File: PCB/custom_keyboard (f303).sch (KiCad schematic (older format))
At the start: 374 parts, among them J1 Conn_01x04, J2 SM04B-SRSS-TB(LF)(SN), J3 Conn_01x03, Q1 2N7002, SW1 SW_Push, U1 SRV05-4, U12 XC6206P332MR, U14 STM32F303CBT6, X1 TestPoint_Small, X2 TestPoint_Small, Y2 8MHz

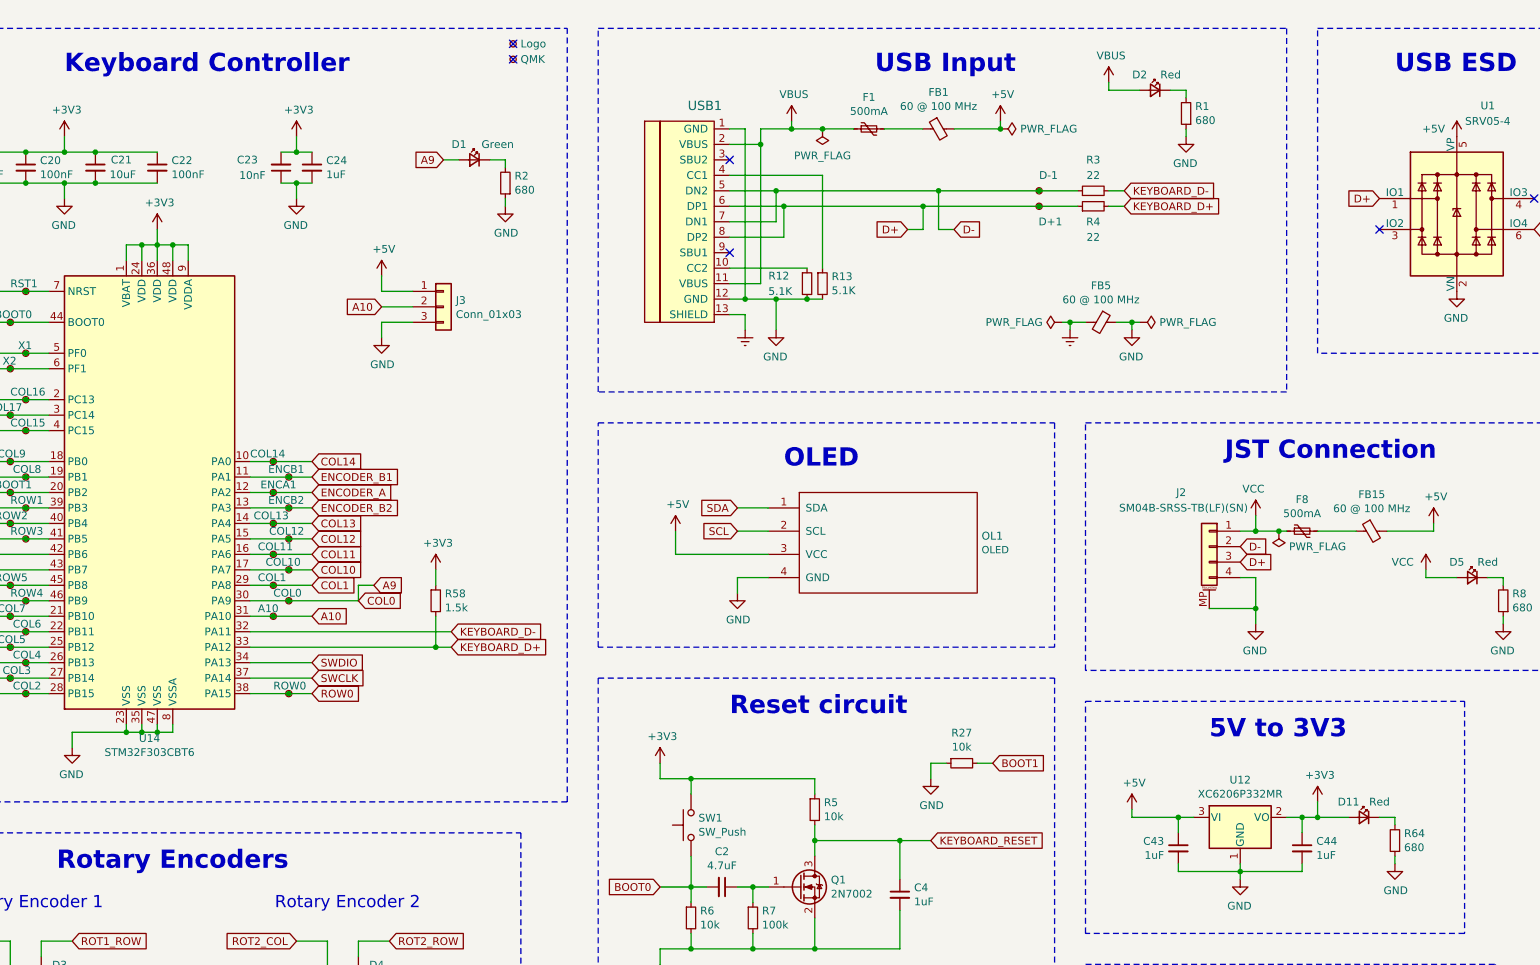
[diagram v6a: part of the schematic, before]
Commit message: Tweaked indicator LED circuit
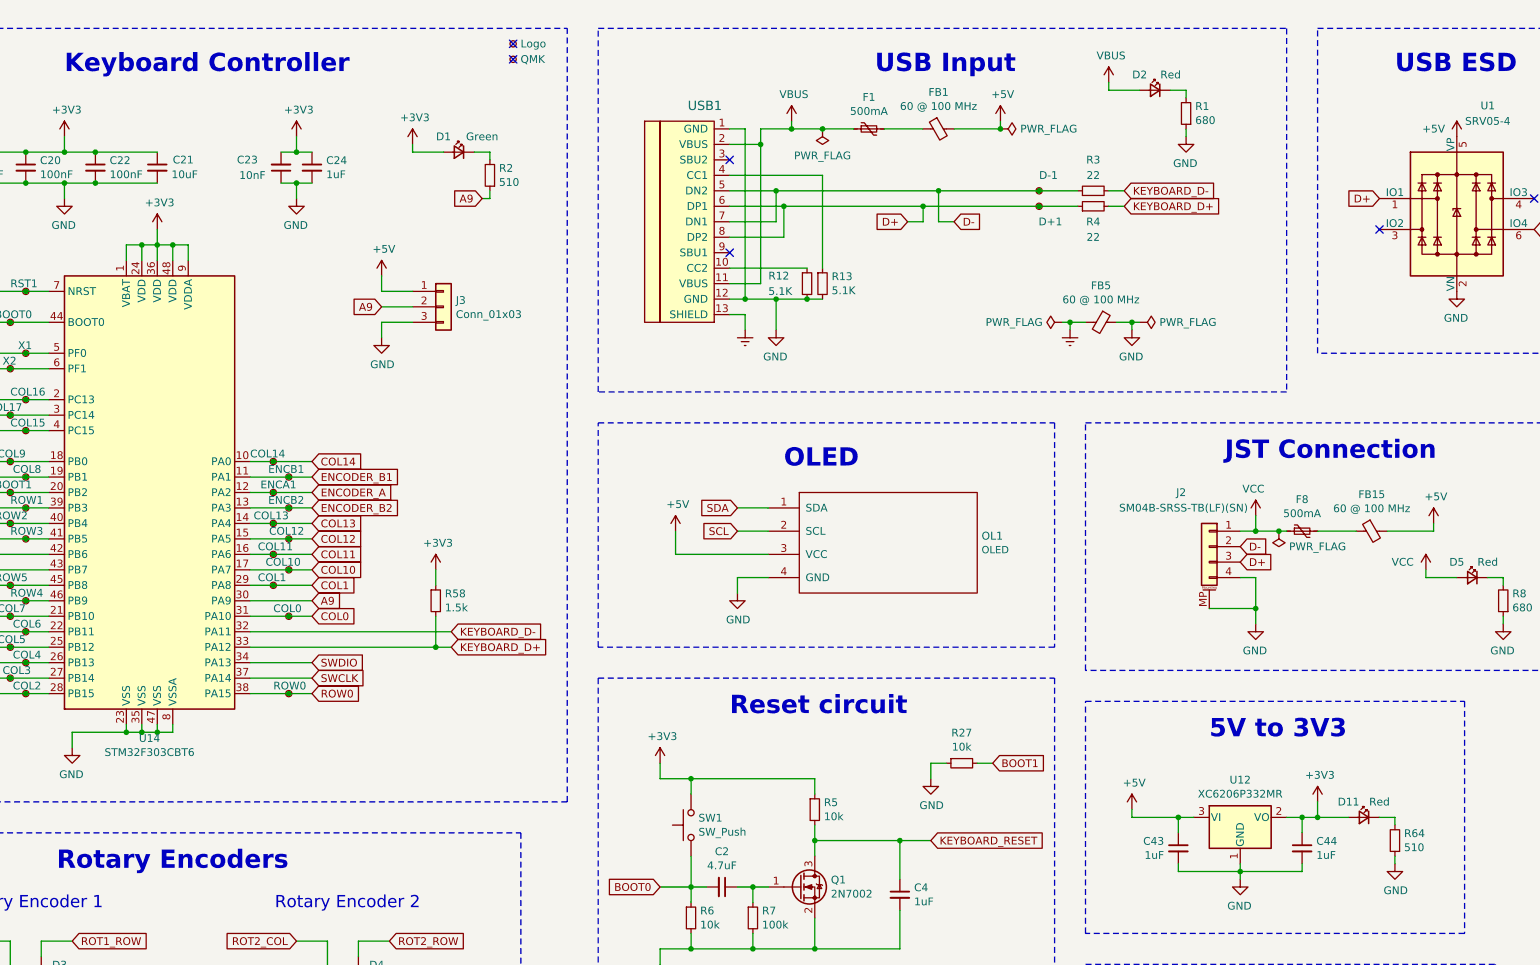
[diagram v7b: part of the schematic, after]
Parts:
- removed A10: TestPoint_Small, TestPoint:TestPoint_THTPad_D1.0mm_Drill0.5mm, symbol Connector:TestPoint_Small
- C1, C11, C13, C18, C19, C20, C22, C6, C8, C9: LCSC Part C49678 -> C28233
- LED1: footprint custom-footprints:MHT151RGBCT_with_outline -> custom-footprints:MHT151RGBCT
- R2, R64: value 680 -> 510; LCSC Part C17798 -> C17734
- Y2: footprint Crystal:Crystal_SMD_HC49-SD -> Crystal:Crystal_SMD_5032-2Pin_5.0x3.2mm; LCSC Part C12674 -> C115962
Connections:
- net +3V3: now also D1.2 (A)
- net A9: now also J3.2 (Pin_2), R2.1; no longer COL0.1, D1.2 (A), MX15.1, MX33.1, MX51.1, MX65.1, MX79.1, ROT1.S1
- net GND: no longer R2.1
- net A10 renamed COL0
- net COL0: now also COL0.1, MX15.1, MX33.1, MX51.1, MX65.1, MX79.1, ROT1.S1; no longer J3.2 (Pin_2)
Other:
- moved on the sheet: C21, C22, COL0, D1, R2

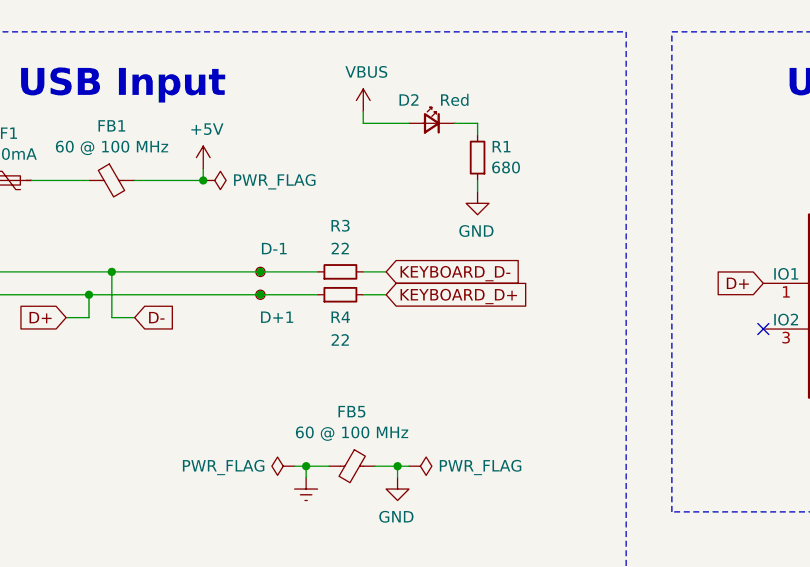
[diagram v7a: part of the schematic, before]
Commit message: Removed 22ohm resistors
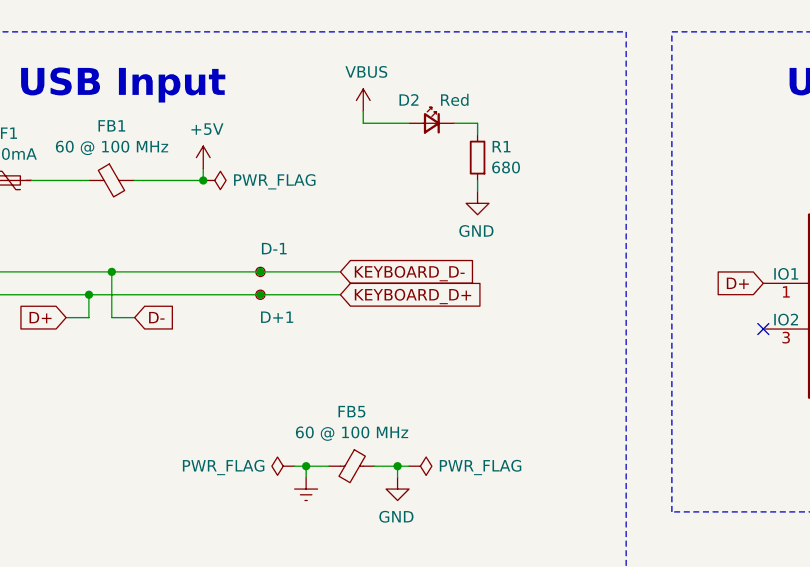
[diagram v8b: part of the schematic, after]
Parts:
- removed R3, R4: 22, Resistor_SMD:R_0805_2012Metric, symbol Device:R_Small
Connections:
- net KEYBOARD_D+ is gone; now on net D+: R58.2, U14.33 (PA12)
- net KEYBOARD_D- is gone; now on net D-: U14.32 (PA11)
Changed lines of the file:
@@
 Wire Notes Line
 	14150 9150 14150 11500
-Text GLabel 13100 10200 2    50   Input ~ 0
+Text GLabel 12900 10200 2    50   Input ~ 0
 KEYBOARD_D-
-Text GLabel 13100 10300 2    50   Input ~ 0
+Text GLabel 12900 10300 2    50   Input ~ 0
 KEYBOARD_D+
 $Comp
-L Device:R_Small R4
-U 1 1 A4110F3E
-P 12900 10300
-F 0 "R4" V 12800 10300 50  0000 C CNN
-F 1 "22" V 12700 10300 50  0000 C CNN
-F 2 "Resistor_SMD:R_0805_2012Metric" H 12900 10300 50  0001 C CNN
-F 3 "~" H 12900 10300 50  0001 C CNN
-F 4 "C17561" H 12900 10300 50  0001 C CNN "LCSC Part"
-	1    12900 10300
-	0    -1   -1   0
-$EndComp
-$Comp
-L Device:R_Small R3
-U 1 1 A4111764
-P 12900 10200
-F 0 "R3" V 13100 10200 50  0000 C CNN
-F 1 "22" V 13000 10200 50  0000 C CNN
-F 2 "Resistor_SMD:R_0805_2012Metric" H 12900 10200 50  0001 C CNN
-F 3 "~" H 12900 10200 50  0001 C CNN
-F 4 "C17561" H 12900 10200 50  0001 C CNN "LCSC Part"
-	1    12900 10200
-	0    -1   -1   0
-$EndComp
-$Comp
 L Connector:TestPoint_Small D-1
 U 1 1 6277D888
@@
 $EndComp
 Connection ~ 12550 10200
-Wire Wire Line
-	12550 10200 12800 10200
 Connection ~ 12550 10300
-Wire Wire Line
-	12550 10300 12800 10300
 $Comp
 L Connector:TestPoint_Small D+1
@@
 $EndComp
 Wire Wire Line
-	13000 10200 13100 10200
-Wire Wire Line
-	13000 10300 13100 10300
-Wire Wire Line
 	10750 9900 10550 9900
 Connection ~ 10750 9900
@@
 	0    -1   -1   0
 $EndComp
+Wire Wire Line
+	12550 10200 12900 10200
+Wire Wire Line
+	12550 10300 12900 10300
 $EndSCHEMATC
